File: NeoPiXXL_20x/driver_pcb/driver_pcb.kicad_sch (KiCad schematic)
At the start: 13 parts, among them U1 WS2811

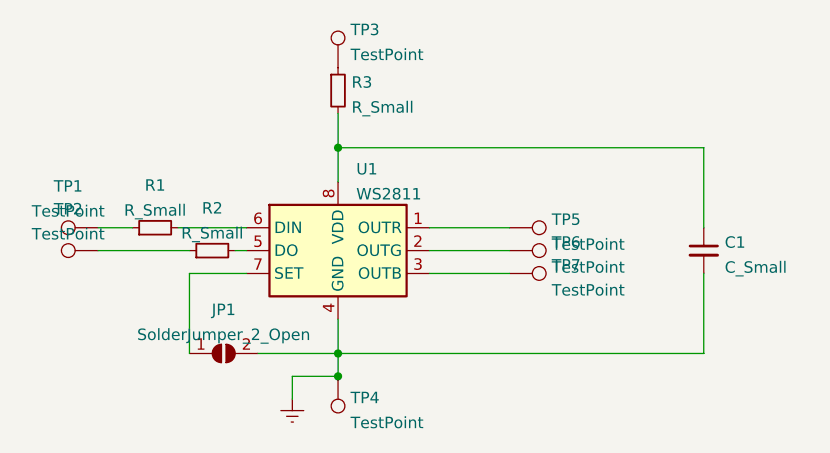
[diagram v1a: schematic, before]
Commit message: include BOM
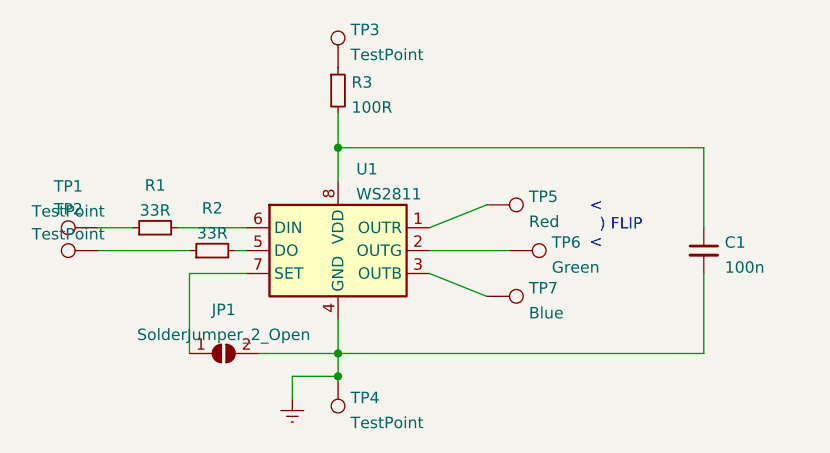
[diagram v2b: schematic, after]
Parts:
- C1: value C_Small -> 100n
- R1, R2: value R_Small -> 33R
- R3: value R_Small -> 100R
- TP5: value TestPoint -> Red
- TP6: value TestPoint -> Green
- TP7: value TestPoint -> Blue
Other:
- note added: "< ) FLIP <"
- moved on the sheet: TP5, TP7
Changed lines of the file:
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@@
     (stroke (width 0) (type default) (color 0 0 0 0))
   )
-  (wire (pts (xy 92.71 85.09) (xy 101.6 85.09))
+  (wire (pts (xy 92.71 85.09) (xy 99.06 82.55))
     (stroke (width 0) (type default) (color 0 0 0 0))
   )
@@
     (stroke (width 0) (type default) (color 0 0 0 0))
   )
-  (wire (pts (xy 92.71 90.17) (xy 101.6 90.17))
+  (wire (pts (xy 92.71 90.17) (xy 99.06 92.71))
     (stroke (width 0) (type default) (color 0 0 0 0))
   )
@@
   (wire (pts (xy 123.19 99.06) (xy 82.55 99.06))
     (stroke (width 0) (type default) (color 0 0 0 0))
+  )
+  (text "< \n  ) FLIP \n<\n" (at 110.49 87.63 0)
+    (effects (font (size 1.27 1.27)) (justify left bottom))
   )
   (symbol (lib_id "power:Earth") (at 77.47 104.14 0) (unit 1)
@@
       (effects (font (size 1.27 1.27)) (justify left))
     )
-    (property "Value" "R_Small" (id 1) (at 84.0486 71.7166 0)
+    (property "Value" "100R" (id 1) (at 84.0486 71.7166 0)
       (effects (font (size 1.27 1.27)) (justify left))
     )
@@
     (pin "2")
   )
-  (symbol (lib_id "Connector:TestPoint") (at 101.6 90.17 270) (unit 1)
-    (in_bom yes) (on_board yes) (fields_autoplaced)
-    (property "Reference" "TP7" (id 0) (at 106.299 89.2615 90)
-      (effects (font (size 1.27 1.27)) (justify left))
-    )
-    (property "Value" "TestPoint" (id 1) (at 106.299 92.0366 90)
-      (effects (font (size 1.27 1.27)) (justify left))
-    )
-    (property "Footprint" "prints:WirePad" (id 2) (at 101.6 95.25 0)
-      (effects (font (size 1.27 1.27)) hide)
-    )
-    (property "Datasheet" "~" (id 3) (at 101.6 95.25 0)
+  (symbol (lib_id "Connector:TestPoint") (at 99.06 92.71 270) (unit 1)
+    (in_bom yes) (on_board yes) (fields_autoplaced)
+    (property "Reference" "TP7" (id 0) (at 103.759 91.8015 90)
+      (effects (font (size 1.27 1.27)) (justify left))
+    )
+    (property "Value" "Blue" (id 1) (at 103.759 94.5766 90)
+      (effects (font (size 1.27 1.27)) (justify left))
+    )
+    (property "Footprint" "prints:WirePad" (id 2) (at 99.06 97.79 0)
+      (effects (font (size 1.27 1.27)) hide)
+    )
+    (property "Datasheet" "~" (id 3) (at 99.06 97.79 0)
       (effects (font (size 1.27 1.27)) hide)
     )
@@
     (in_bom yes) (on_board yes) (fields_autoplaced)
     (property "Reference" "R2" (id 0) (at 68.58 82.9269 90))
-    (property "Value" "R_Small" (id 1) (at 68.58 85.702 90))
+    (property "Value" "33R" (id 1) (at 68.58 85.702 90))
     (property "Footprint" "Resistor_SMD:R_0603_1608Metric_Pad0.98x0.95mm_HandSolder" (id 2) (at 68.58 87.63 0)
       (effects (font (size 1.27 1.27)) hide)
@@
     (in_bom yes) (on_board yes) (fields_autoplaced)
     (property "Reference" "R1" (id 0) (at 62.23 80.3869 90))
-    (property "Value" "R_Small" (id 1) (at 62.23 83.162 90))
+    (property "Value" "33R" (id 1) (at 62.23 83.162 90))
     (property "Footprint" "Resistor_SMD:R_0603_1608Metric_Pad0.98x0.95mm_HandSolder" (id 2) (at 62.23 85.09 0)
       (effects (font (size 1.27 1.27)) hide)
@@
     (pin "2")
   )
-  (symbol (lib_id "Connector:TestPoint") (at 101.6 85.09 270) (unit 1)
-    (in_bom yes) (on_board yes) (fields_autoplaced)
-    (property "Reference" "TP5" (id 0) (at 106.299 84.1815 90)
-      (effects (font (size 1.27 1.27)) (justify left))
-    )
-    (property "Value" "TestPoint" (id 1) (at 106.299 86.9566 90)
-      (effects (font (size 1.27 1.27)) (justify left))
-    )
-    (property "Footprint" "prints:WirePad" (id 2) (at 101.6 90.17 0)
-      (effects (font (size 1.27 1.27)) hide)
-    )
-    (property "Datasheet" "~" (id 3) (at 101.6 90.17 0)
+  (symbol (lib_id "Connector:TestPoint") (at 99.06 82.55 270) (unit 1)
+    (in_bom yes) (on_board yes) (fields_autoplaced)
+    (property "Reference" "TP5" (id 0) (at 103.759 81.6415 90)
+      (effects (font (size 1.27 1.27)) (justify left))
+    )
+    (property "Value" "Red" (id 1) (at 103.759 84.4166 90)
+      (effects (font (size 1.27 1.27)) (justify left))
+    )
+    (property "Footprint" "prints:WirePad" (id 2) (at 99.06 87.63 0)
+      (effects (font (size 1.27 1.27)) hide)
+    )
+    (property "Datasheet" "~" (id 3) (at 99.06 87.63 0)
       (effects (font (size 1.27 1.27)) hide)
     )
@@
       (effects (font (size 1.27 1.27)) (justify left))
     )
-    (property "Value" "TestPoint" (id 1) (at 106.299 89.4966 90)
+    (property "Value" "Green" (id 1) (at 106.299 89.4966 90)
       (effects (font (size 1.27 1.27)) (justify left))
     )
@@
       (effects (font (size 1.27 1.27)) (justify left))
     )
-    (property "Value" "C_Small" (id 1) (at 125.5141 89.5029 0)
+    (property "Value" "100n" (id 1) (at 125.5141 89.5029 0)
       (effects (font (size 1.27 1.27)) (justify left))
     )
@@
     )
     (path "/f9e04293-6ec5-4486-b9e9-2a4a8ca2cad3"
-      (reference "C1") (unit 1) (value "C_Small") (footprint "Capacitor_SMD:C_0603_1608Metric_Pad1.08x0.95mm_HandSolder")
+      (reference "C1") (unit 1) (value "100n") (footprint "Capacitor_SMD:C_0603_1608Metric_Pad1.08x0.95mm_HandSolder")
     )
     (path "/56771477-e1fd-44cc-9e62-f2d43d95052a"
@@
     )
     (path "/49a73562-fc7a-44a1-8562-76326a6322ae"
-      (reference "R1") (unit 1) (value "R_Small") (footprint "Resistor_SMD:R_0603_1608Metric_Pad0.98x0.95mm_HandSolder")
+      (reference "R1") (unit 1) (value "33R") (footprint "Resistor_SMD:R_0603_1608Metric_Pad0.98x0.95mm_HandSolder")
     )
     (path "/3a71e4f8-929c-487e-bcb7-5543a8ce30cd"
-      (reference "R2") (unit 1) (value "R_Small") (footprint "Resistor_SMD:R_0603_1608Metric_Pad0.98x0.95mm_HandSolder")
+      (reference "R2") (unit 1) (value "33R") (footprint "Resistor_SMD:R_0603_1608Metric_Pad0.98x0.95mm_HandSolder")
     )
     (path "/2019d1cb-3f44-4350-b567-07ec343b7ded"
-      (reference "R3") (unit 1) (value "R_Small") (footprint "Resistor_SMD:R_0603_1608Metric_Pad0.98x0.95mm_HandSolder")
+      (reference "R3") (unit 1) (value "100R") (footprint "Resistor_SMD:R_0603_1608Metric_Pad0.98x0.95mm_HandSolder")
     )
     (path "/6e05b346-f5da-4f41-a6d5-03287b6549d7"
@@
     )
     (path "/5cdadff0-5a09-46c9-957a-1769ea0320b7"
-      (reference "TP5") (unit 1) (value "TestPoint") (footprint "prints:WirePad")
+      (reference "TP5") (unit 1) (value "Red") (footprint "prints:WirePad")
     )
     (path "/74879186-cb05-4567-bafd-12b2abc3fb90"
-      (reference "TP6") (unit 1) (value "TestPoint") (footprint "prints:WirePad")
+      (reference "TP6") (unit 1) (value "Green") (footprint "prints:WirePad")
     )
     (path "/386d13b5-3a15-48e0-abd4-a201beb5cd69"
-      (reference "TP7") (unit 1) (value "TestPoint") (footprint "prints:WirePad")
+      (reference "TP7") (unit 1) (value "Blue") (footprint "prints:WirePad")
     )
     (path "/15189cef-9045-423b-b4f6-a763d4e75704"

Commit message: Update driver for correct LED placement
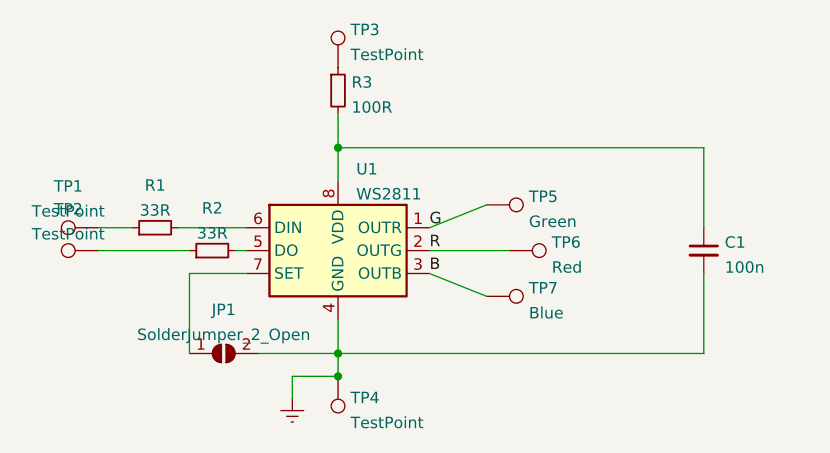
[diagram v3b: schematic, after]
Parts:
- TP5: value Red -> Green
- TP6: value Green -> Red
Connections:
- net G: now reaches TP5.1, U1.1 (OUTR)
- net R: now reaches TP6.1, U1.2 (OUTG)
- net B: now reaches TP7.1, U1.3 (OUTB)
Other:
- note removed: "< ) FLIP <"
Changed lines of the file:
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@@
     (stroke (width 0) (type default) (color 0 0 0 0))
   )
-  (text "< \n  ) FLIP \n<\n" (at 110.49 87.63 0)
+  (label "G" (at 92.71 85.09 0)
+    (effects (font (size 1.27 1.27)) (justify left bottom))
+  )
+  (label "B" (at 92.71 90.17 0)
+    (effects (font (size 1.27 1.27)) (justify left bottom))
+  )
+  (label "R" (at 92.71 87.63 0)
     (effects (font (size 1.27 1.27)) (justify left bottom))
   )
@@
       (effects (font (size 1.27 1.27)) (justify left))
     )
-    (property "Value" "Red" (id 1) (at 103.759 84.4166 90)
+    (property "Value" "Green" (id 1) (at 103.759 84.4166 90)
       (effects (font (size 1.27 1.27)) (justify left))
     )
@@
       (effects (font (size 1.27 1.27)) (justify left))
     )
-    (property "Value" "Green" (id 1) (at 106.299 89.4966 90)
+    (property "Value" "Red" (id 1) (at 106.299 89.4966 90)
       (effects (font (size 1.27 1.27)) (justify left))
     )
@@
     )
     (path "/5cdadff0-5a09-46c9-957a-1769ea0320b7"
-      (reference "TP5") (unit 1) (value "Red") (footprint "prints:WirePad")
+      (reference "TP5") (unit 1) (value "Green") (footprint "prints:WirePad")
     )
     (path "/74879186-cb05-4567-bafd-12b2abc3fb90"
-      (reference "TP6") (unit 1) (value "Green") (footprint "prints:WirePad")
+      (reference "TP6") (unit 1) (value "Red") (footprint "prints:WirePad")
     )
     (path "/386d13b5-3a15-48e0-abd4-a201beb5cd69"
